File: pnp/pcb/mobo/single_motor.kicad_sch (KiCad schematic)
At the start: 8 parts, among them M1 Stepper_Motor

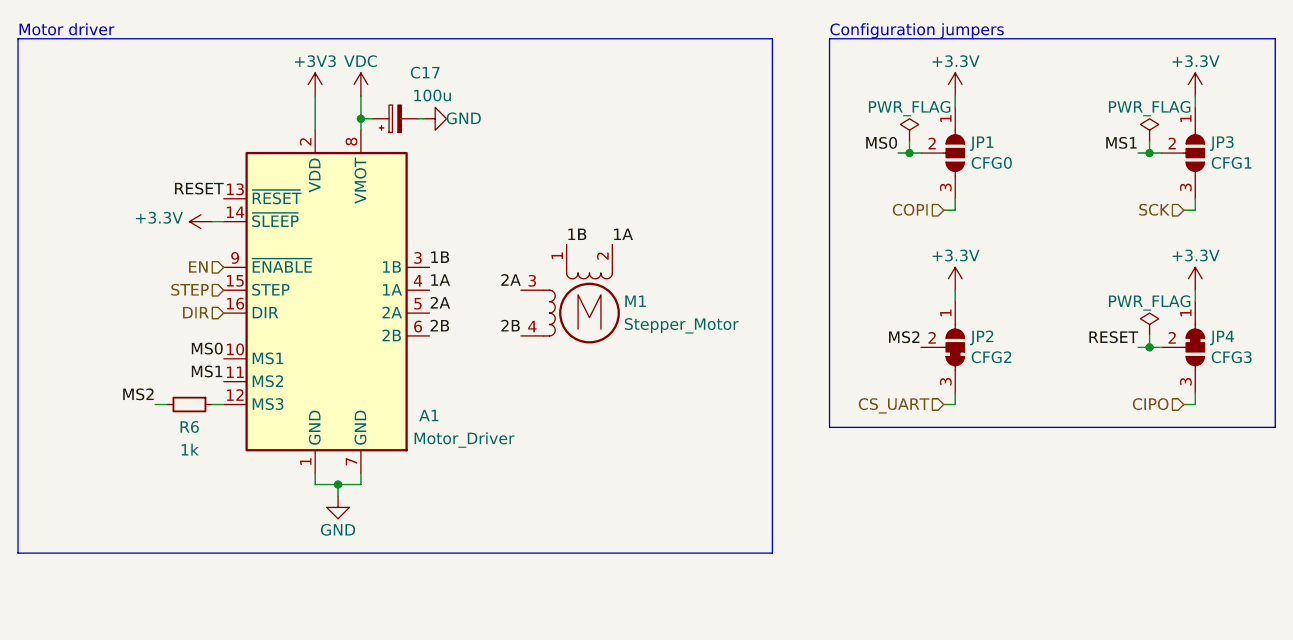
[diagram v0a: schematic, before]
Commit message: first commit of rev04 mobo beta 0. makes solder-selectable jumpers on back side of board not jumped to work with kit drivers, y2 motor port rotated correctly, moves traces out from underneath solder jumpers, adds 0 ohm jumpers to bypass the usb hub, adds 4 pin DIN connector for power, adds large decoupling cap on power supply input to decrease rippling, changes diode choice for 5v multiplexer to one already in the BOM, flips resistors on mos1 to be less confusing
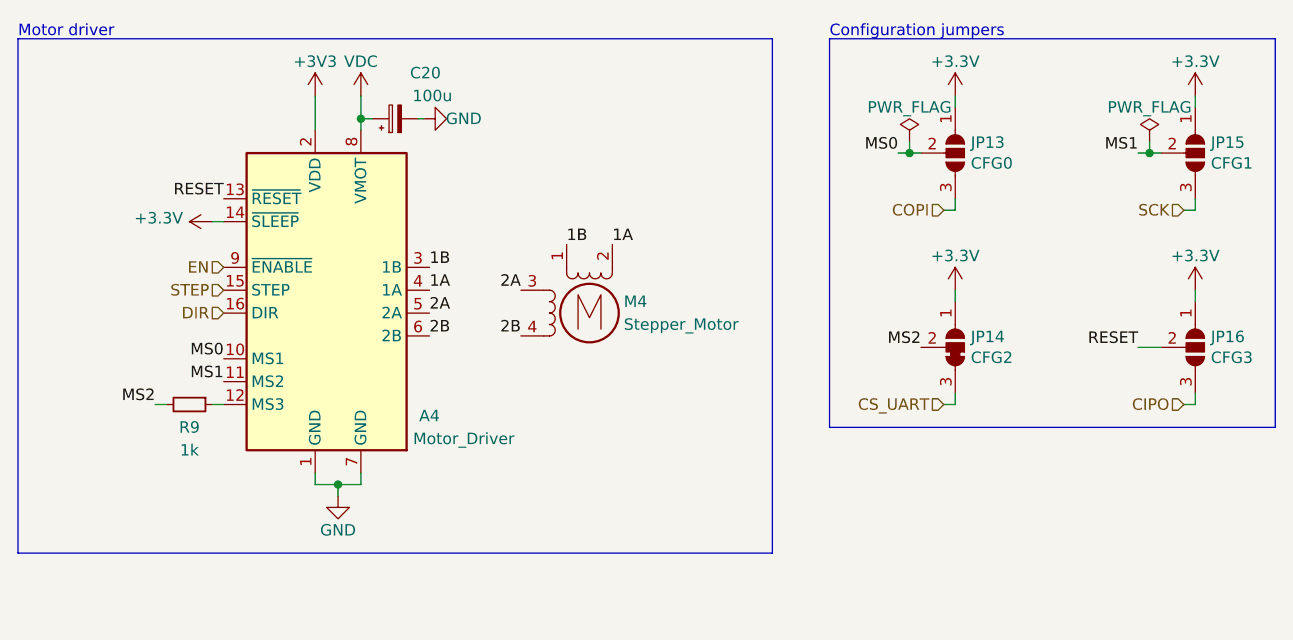
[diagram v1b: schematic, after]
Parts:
- removed JP4: CFG3, Jumper:SolderJumper-3_P1.3mm_Bridged12_RoundedPad1.0x1.5mm, symbol Jumper:SolderJumper_3_Bridged12
- added JP16: CFG3, Jumper:SolderJumper-3_P1.3mm_Open_RoundedPad1.0x1.5mm, symbol Jumper:SolderJumper_3_Open
- renumbered A1 to A4, C17 to C20, JP1 to JP13, JP2 to JP14, JP3 to JP15, M1 to M4, R6 to R9
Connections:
- net +3V3: now also JP16.1 (A)
- net CIPO: now also JP16.3 (B)
- net RESET: now also JP16.2 (C)

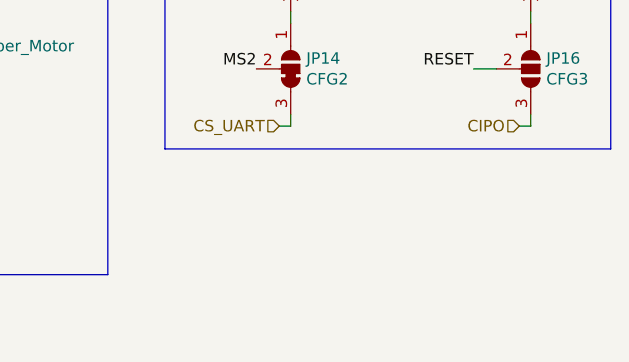
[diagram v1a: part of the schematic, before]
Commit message: another huge chunk of work on rev04 of the mobo. breaks out diag and index pin for TMC2209 sensorless homing. reduces unique part count by consolidating resistor values where possible. replaces full ADC pipeline with monolithic I2C vacuum sensor and an I2C multiplexer due to address collision issues with two sensors. adds solder selectable jumpers for selecting whether an axis uses switch or TMC homing. redoes lots of routing of the SPI lines up to the stepper drivers.
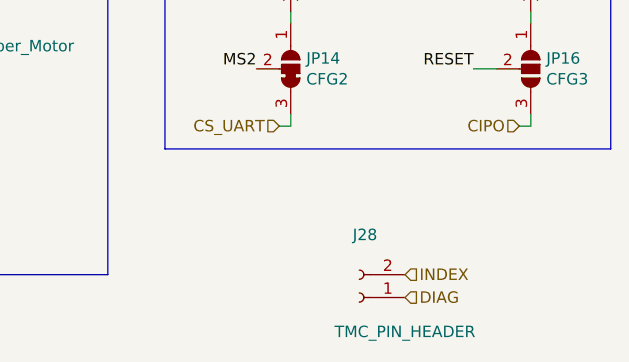
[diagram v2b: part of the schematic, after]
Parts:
- added J28: TMC_PIN_HEADER, Connector_PinHeader_2.54mm:PinHeader_1x02_P2.54mm_Vertical, symbol Connector:Conn_01x02_Female
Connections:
- new net DIAG: J28.1 (Pin_1)
- new net INDEX: J28.2 (Pin_2)
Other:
- company: (none) -> Opulo
- title: Motor -> LumenPnP Motherboard
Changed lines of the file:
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@@
   (paper "A4")
   (title_block
-    (title "Motor")
+    (title "LumenPnP Motherboard")
     (date "2022-03-29")
     (rev "003")
+    (company "Opulo")
   )
   (junction (at 115.57 86.36) (diameter 0) (color 0 0 0 0)
@@
     (effects (font (size 1.27 1.27)) (justify right))
   )
+  (hierarchical_label "DIAG" (shape input) (at 194.31 137.16 0)
+    (effects (font (size 1.27 1.27)) (justify left))
+  )
   (hierarchical_label "DIR" (shape input) (at 100.33 107.95 180)
     (effects (font (size 1.27 1.27)) (justify right))
@@
   (hierarchical_label "SCK" (shape input) (at 207.01 96.52 180)
     (effects (font (size 1.27 1.27)) (justify right))
+  )
+  (hierarchical_label "INDEX" (shape input) (at 194.31 134.62 0)
+    (effects (font (size 1.27 1.27)) (justify left))
   )
   (hierarchical_label "COPI" (shape input) (at 180.34 96.52 180)
@@
     (pin "3")
   )
+  (symbol (lib_id "Connector:Conn_01x02_Female") (at 189.23 137.16 180)
+    (in_bom yes) (on_board yes)
+    (property "Reference" "J28" (id 0) (at 189.865 130.1963 0))
+    (property "Value" "TMC_PIN_HEADER" (id 1) (at 194.31 140.97 0))
+    (property "Footprint" "Connector_PinHeader_2.54mm:PinHeader_1x02_P2.54mm_Vertical" (id 2) (at 189.23 137.16 0)
+      (effects (font (size 1.27 1.27)) hide)
+    )
+    (property "Datasheet" "~" (id 3) (at 189.23 137.16 0)
+      (effects (font (size 1.27 1.27)) hide)
+    )
+    (pin "1")
+    (pin "2")
+  )
 )

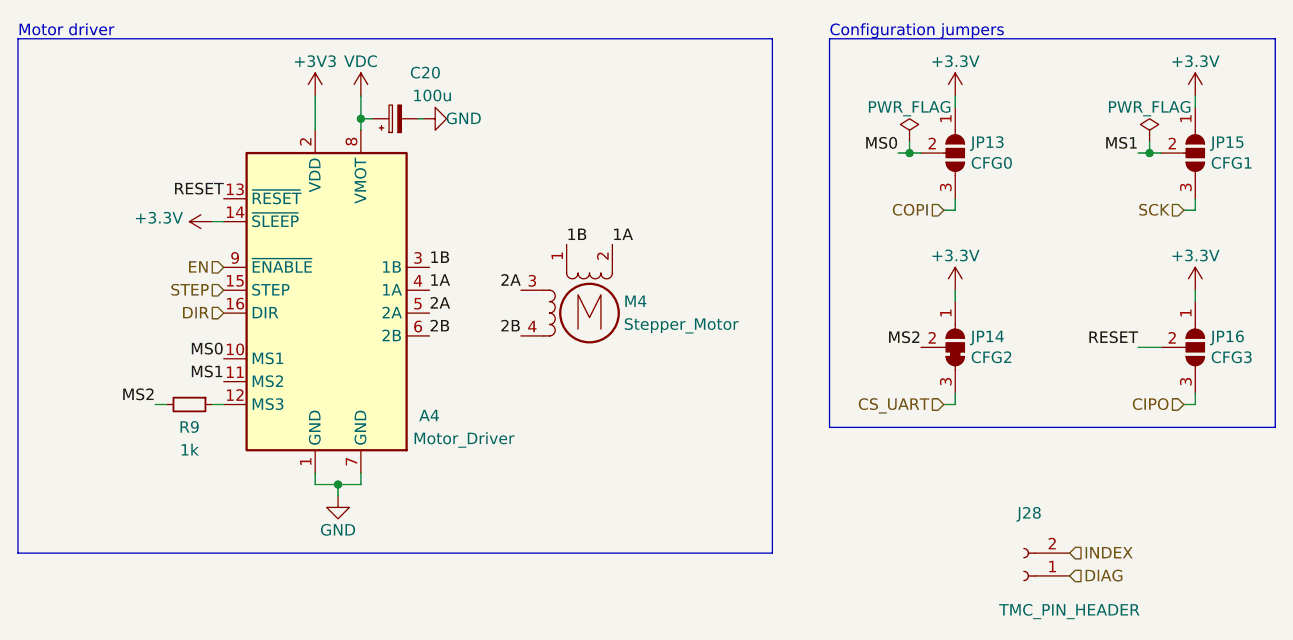
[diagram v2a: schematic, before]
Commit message: adds all missing 3d models, including custom model for the vacuum sensor. corrects wrong model for the diag and index pin header for the stepper drivers. changes the vacuum sensors to 3.3v power instead of 5v. cleans up some silkscreen.
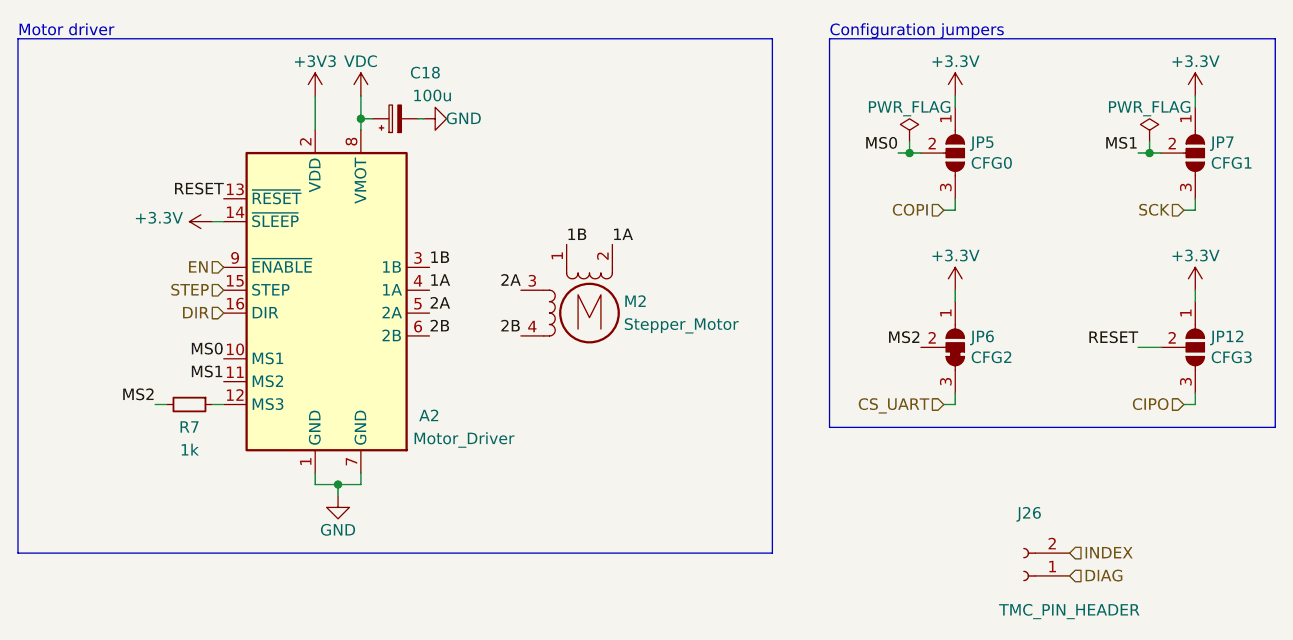
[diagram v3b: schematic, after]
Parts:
- J26: renamed from J28; footprint Connector_PinHeader_2.54mm:PinHeader_1x02_P2.54mm_Vertical -> Connector_PinSocket_2.54mm:PinSocket_1x02_P2.54mm_Vertical
- renumbered A4 to A2, C20 to C18, JP16 to JP12, JP13 to JP5, JP14 to JP6, JP15 to JP7, M4 to M2, R9 to R7
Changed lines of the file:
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@@
   (symbol (lib_id "power:+3.3V") (at 208.28 105.41 0)
     (in_bom yes) (on_board yes)
-    (property "Reference" "#PWR0213" (id 0) (at 208.28 109.22 0)
+    (property "Reference" "#PWR0181" (id 0) (at 208.28 109.22 0)
       (effects (font (size 1.27 1.27)) hide)
     )
@@
   (symbol (lib_id "Device:R_Small") (at 96.52 118.11 270)
     (in_bom yes) (on_board yes)
-    (property "Reference" "R9" (id 0) (at 96.52 120.65 90))
+    (property "Reference" "R7" (id 0) (at 96.52 120.65 90))
     (property "Value" "1k" (id 1) (at 96.52 123.19 90))
     (property "Footprint" "Resistor_SMD:R_0805_2012Metric" (id 2) (at 96.52 116.332 90)
@@
   (symbol (lib_id "power:+3.3V") (at 181.61 83.82 0)
     (in_bom yes) (on_board yes)
-    (property "Reference" "#PWR0214" (id 0) (at 181.61 87.63 0)
+    (property "Reference" "#PWR0182" (id 0) (at 181.61 87.63 0)
       (effects (font (size 1.27 1.27)) hide)
     )
@@
   (symbol (lib_id "power:GND") (at 113.03 128.27 0)
     (in_bom yes) (on_board yes)
-    (property "Reference" "#PWR0220" (id 0) (at 113.03 134.62 0)
+    (property "Reference" "#PWR0202" (id 0) (at 113.03 134.62 0)
       (effects (font (size 1.27 1.27)) hide)
     )
@@
   (symbol (lib_id "power:+3.3V") (at 99.06 97.79 90)
     (in_bom yes) (on_board yes)
-    (property "Reference" "#PWR0217" (id 0) (at 102.87 97.79 0)
+    (property "Reference" "#PWR0199" (id 0) (at 102.87 97.79 0)
       (effects (font (size 1.27 1.27)) hide)
     )
@@
   (symbol (lib_id "power:PWR_FLAG") (at 203.2 88.9 0)
     (in_bom yes) (on_board yes)
-    (property "Reference" "#FLG0113" (id 0) (at 203.2 86.995 0)
+    (property "Reference" "#FLG0107" (id 0) (at 203.2 86.995 0)
       (effects (font (size 1.27 1.27)) hide)
     )
@@
   (symbol (lib_id "power:+3.3V") (at 181.61 105.41 0)
     (in_bom yes) (on_board yes)
-    (property "Reference" "#PWR0212" (id 0) (at 181.61 109.22 0)
+    (property "Reference" "#PWR0180" (id 0) (at 181.61 109.22 0)
       (effects (font (size 1.27 1.27)) hide)
     )
@@
   (symbol (lib_id "Driver_Motor:Pololu_Breakout_A4988") (at 110.49 105.41 0)
     (in_bom yes) (on_board yes)
-    (property "Reference" "A4" (id 0) (at 123.19 119.38 0))
+    (property "Reference" "A2" (id 0) (at 123.19 119.38 0))
     (property "Value" "Motor_Driver" (id 1) (at 127 121.92 0))
     (property "Footprint" "Module:Pololu_Breakout-16_15.2x20.3mm" (id 2) (at 117.475 124.46 0)
@@
   (symbol (lib_id "power:GND") (at 122.555 86.36 90)
     (in_bom yes) (on_board yes)
-    (property "Reference" "#PWR0216" (id 0) (at 128.905 86.36 0)
+    (property "Reference" "#PWR0184" (id 0) (at 128.905 86.36 0)
       (effects (font (size 1.27 1.27)) hide)
     )
@@
   (symbol (lib_id "power:+3.3V") (at 208.28 83.82 0)
     (in_bom yes) (on_board yes)
-    (property "Reference" "#PWR0215" (id 0) (at 208.28 87.63 0)
+    (property "Reference" "#PWR0183" (id 0) (at 208.28 87.63 0)
       (effects (font (size 1.27 1.27)) hide)
     )
@@
   (symbol (lib_id "power:VDC") (at 115.57 83.82 0)
     (in_bom yes) (on_board yes)
-    (property "Reference" "#PWR0219" (id 0) (at 115.57 86.36 0)
+    (property "Reference" "#PWR0201" (id 0) (at 115.57 86.36 0)
       (effects (font (size 1.27 1.27)) hide)
     )
@@
   (symbol (lib_id "Device:C_Polarized_Small") (at 119.38 86.36 90)
     (in_bom yes) (on_board yes)
-    (property "Reference" "C20" (id 0) (at 124.46 81.28 90)
+    (property "Reference" "C18" (id 0) (at 124.46 81.28 90)
       (effects (font (size 1.27 1.27)) (justify left))
     )
@@
   (symbol (lib_id "Jumper:SolderJumper_3_Open") (at 181.61 90.17 270)
     (in_bom yes) (on_board yes)
-    (property "Reference" "JP13" (id 0) (at 183.3372 89.0016 90)
+    (property "Reference" "JP5" (id 0) (at 183.3372 89.0016 90)
       (effects (font (size 1.27 1.27)) (justify left))
     )
@@
   (symbol (lib_id "power:PWR_FLAG") (at 176.53 88.9 0)
     (in_bom yes) (on_board yes)
-    (property "Reference" "#FLG0115" (id 0) (at 176.53 86.995 0)
+    (property "Reference" "#FLG0109" (id 0) (at 176.53 86.995 0)
       (effects (font (size 1.27 1.27)) hide)
     )
@@
   (symbol (lib_id "Jumper:SolderJumper_3_Open") (at 208.28 111.76 270)
     (in_bom yes) (on_board yes)
-    (property "Reference" "JP16" (id 0) (at 210.0072 110.5916 90)
+    (property "Reference" "JP12" (id 0) (at 210.0072 110.5916 90)
       (effects (font (size 1.27 1.27)) (justify left))
     )
@@
   (symbol (lib_id "power:+3V3") (at 110.49 83.82 0)
     (in_bom yes) (on_board yes)
-    (property "Reference" "#PWR0218" (id 0) (at 110.49 87.63 0)
+    (property "Reference" "#PWR0200" (id 0) (at 110.49 87.63 0)
       (effects (font (size 1.27 1.27)) hide)
     )
@@
   (symbol (lib_id "index:SolderJumper_3_Bridged23") (at 181.61 111.76 270) (mirror x)
     (in_bom yes) (on_board yes)
-    (property "Reference" "JP14" (id 0) (at 183.3372 110.5916 90)
+    (property "Reference" "JP6" (id 0) (at 183.3372 110.5916 90)
       (effects (font (size 1.27 1.27)) (justify left))
     )
@@
   (symbol (lib_id "Motor:Stepper_Motor_bipolar") (at 140.97 107.95 0)
     (in_bom yes) (on_board yes)
-    (property "Reference" "M4" (id 0) (at 144.78 106.68 0)
+    (property "Reference" "M2" (id 0) (at 144.78 106.68 0)
       (effects (font (size 1.27 1.27)) (justify left))
     )
@@
   (symbol (lib_id "Jumper:SolderJumper_3_Open") (at 208.28 90.17 270)
     (in_bom yes) (on_board yes)
-    (property "Reference" "JP15" (id 0) (at 210.0072 89.0016 90)
+    (property "Reference" "JP7" (id 0) (at 210.0072 89.0016 90)
       (effects (font (size 1.27 1.27)) (justify left))
     )
@@
   (symbol (lib_id "Connector:Conn_01x02_Female") (at 189.23 137.16 180)
     (in_bom yes) (on_board yes)
-    (property "Reference" "J28" (id 0) (at 189.865 130.1963 0))
+    (property "Reference" "J26" (id 0) (at 189.865 130.1963 0))
     (property "Value" "TMC_PIN_HEADER" (id 1) (at 194.31 140.97 0))
-    (property "Footprint" "Connector_PinHeader_2.54mm:PinHeader_1x02_P2.54mm_Vertical" (id 2) (at 189.23 137.16 0)
-      (effects (font (size 1.27 1.27)) hide)
-    )
+    (property "Footprint" "Connector_PinSocket_2.54mm:PinSocket_1x02_P2.54mm_Vertical" (id 2) (at 189.23 137.16 0)
+      (effects (font (size 1.27 1.27)) hide)
+    )
